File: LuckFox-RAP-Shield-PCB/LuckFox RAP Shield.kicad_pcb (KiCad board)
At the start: 2 copper layers, 45 x 62.6 mm, 8 parts, among them J1 LuckFox_Pico_Mini_Connector, J2 External_5V_Input_from_Buck_M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, U2 W5500_Ethernet_Module_DNP_on_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

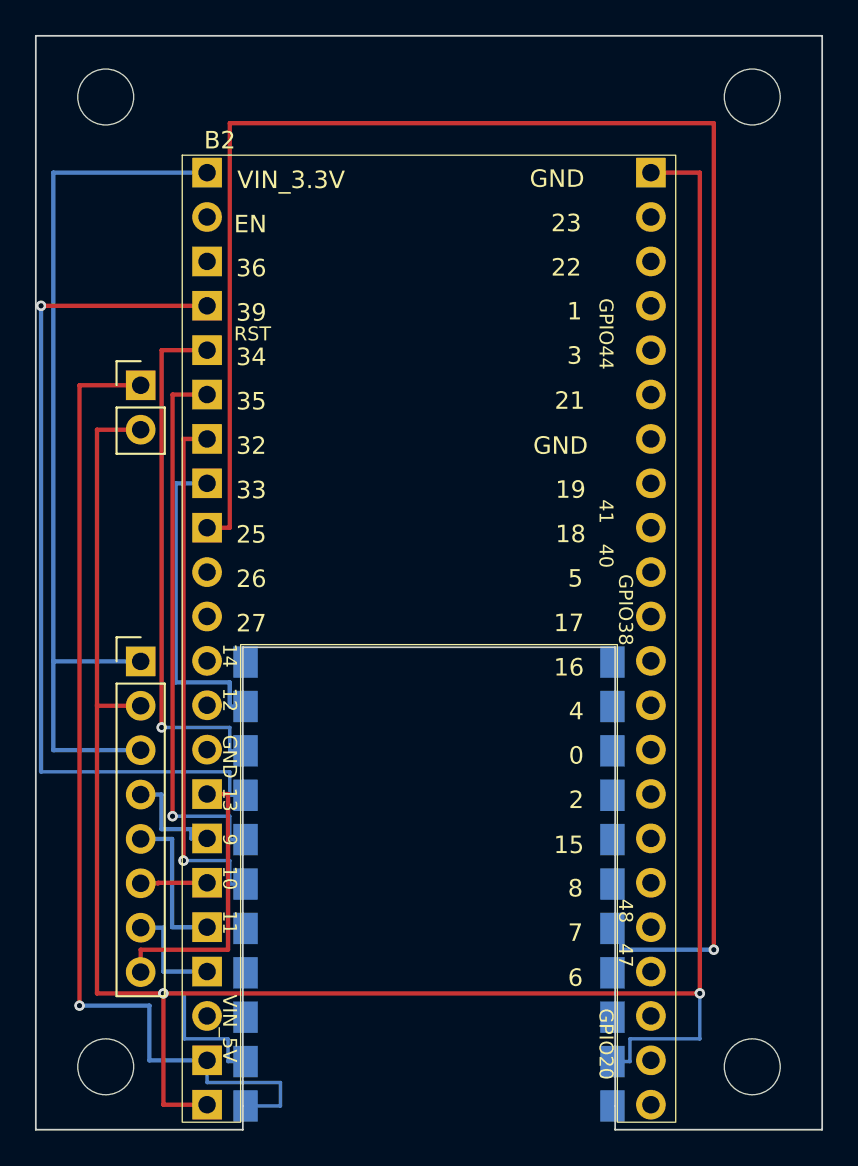
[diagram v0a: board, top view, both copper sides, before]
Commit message: Cut the real LuckFox nesting slot into the board outline, reroute GND/+5V_RAIL around it
LuckFox Pico Mini has an SD card slot, so it can't sit flush -- it
needs to actually nest into a cut opening in the shield (castellated
edge pads lap-solder where the module's edge meets the shield at the
slot boundary), not just be surface-soldered on top. The J1
footprint's own U-shaped Edge.Cuts lines already describe this slot
correctly, but its description explicitly warns "it is not
automatically merged with your board outline" -- and it never was.
Added the 3 missing lines to the top-level board outline so the slot
is now real (confirmed by re-deriving the closed outline: main
outline -> up J1's right edge -> across its top -> down its left
edge -> back to the main outline's own bottom notch).

Two nets previously ran straight through where that slot now is:
- GND's main trunk (116.5,129.8)-(151,129.8) crossed the entire
  21.3mm width of it. Rerouted above it instead: north to Y=99.34
  (clear of J2's pads to the south and B2/DATA_RDY's pins to the
  south-east), across on B.Cu (avoiding SPI0's F.Cu lanes at
  X=120.2/120.825/121.45, which occupy this same row), back down to
  the original via at (151,129.8) on the east side.
- +5V_RAIL's approach into J1.1 jogged out to X=127, well inside the
  slot, before turning back to the pad at X=125. Straightened to a
  short stub from X=124.1 (matching the established SPI0-style
  approach lane), only 0.15mm past the slot's real edge -- consistent
  with how J1's other pads (castellated, meant to straddle the edge)
  are already approached.

The short stubs already reaching J1's other pads (SPI0, DATA_RDY,
SLAVE_RDY_OUT, GND's other two J1 connections) were left as-is --
each only overhangs ~0.15-0.9mm past the real edge to reach a pad
that's itself meant to sit at that edge, same as J1's existing
castellated-pad DRU exception already covers for copper clearance.

Re-verified the new routing offline against every existing pad,
t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
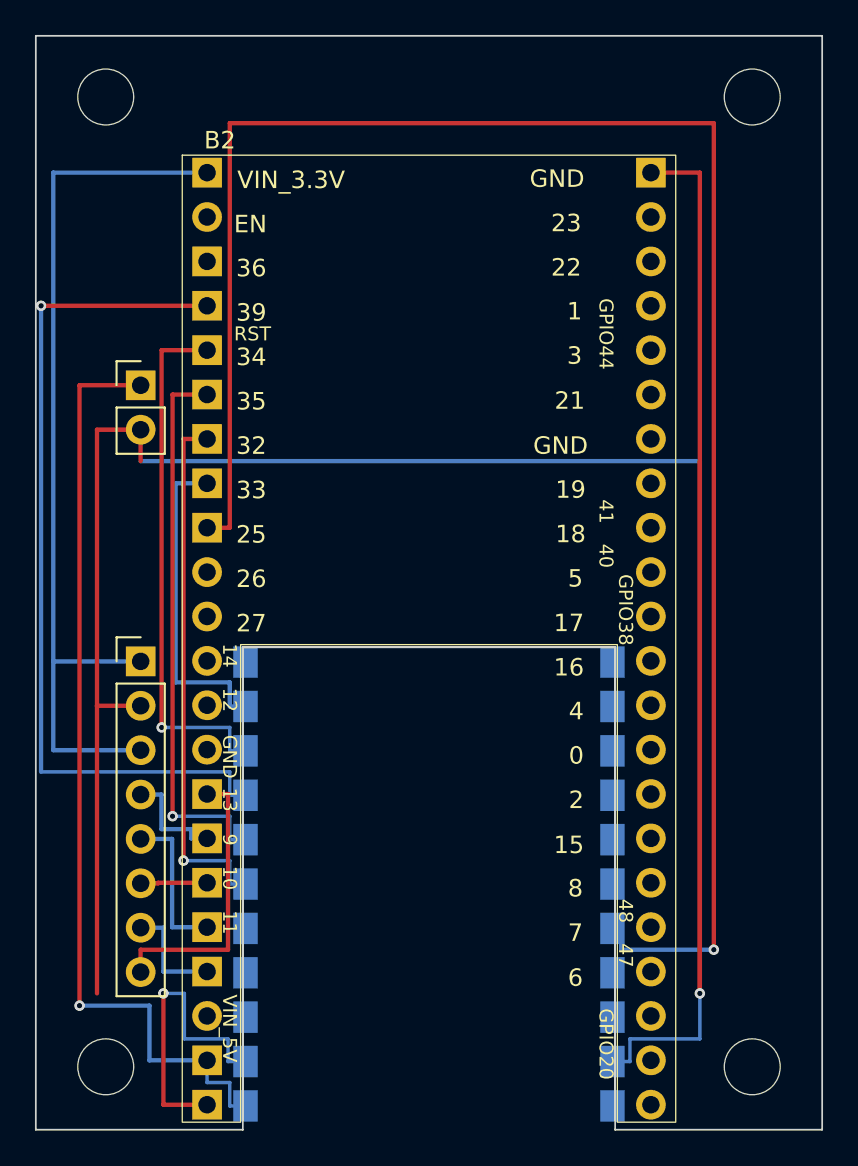
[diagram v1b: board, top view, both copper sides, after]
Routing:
- net GND: track 147.9 -> 177.7 mm
- net +5V_RAIL: track 58.2 -> 54.2 mm
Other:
- outline, holes or cut-outs redrawn
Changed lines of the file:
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@@
+	)
+	(gr_line
+		(start 146.15 136.24)
+		(end 146.15 109.99)
+		(stroke
+			(width 0.1)
+			(type solid)
+		)
+		(layer "Edge.Cuts")
+	)
+	(gr_line
+		(start 146.15 109.99)
+		(end 124.85 109.99)
+		(stroke
+			(width 0.1)
+			(type solid)
+		)
+		(layer "Edge.Cuts")
+	)
+	(gr_line
+		(start 124.85 109.99)
+		(end 124.85 136.24)
+		(stroke
+			(width 0.1)
+			(type solid)
+		)
+		(layer "Edge.Cuts")
 	)
 	(gr_line
@@
 	)
 	(segment
-		(start 127 134.9)
-		(end 127 136.24)
-		(width 0.2)
-		(layer "B.Cu")
-		(net "+5V_RAIL")
-	)
-	(segment
 		(start 119.5 133.63)
 		(end 122.8 133.63)
@@
 	)
 	(segment
-		(start 127 136.24)
-		(end 125 136.24)
-		(width 0.2)
-		(layer "B.Cu")
-		(net "+5V_RAIL")
-	)
-	(segment
-		(start 122.8 134.9)
-		(end 127 134.9)
-		(width 0.2)
-		(layer "B.Cu")
-		(net "+5V_RAIL")
-	)
-	(segment
 		(start 115.5 130.5)
 		(end 119.5 130.5)
@@
 	)
 	(segment
-		(start 116.5 129.8)
-		(end 151 129.8)
-		(width 0.25)
-		(layer "F.Cu")
-		(net "GND")
-	)
-	(segment
 		(start 120.3 129.8)
 		(end 120.3 136.17)
@@
 		(net "Net-(B2-GPIO16_SLAVE_RDY_OUT)")
 	)
+	(segment
+		(start 119.0 97.54)
+		(end 119.0 99.34)
+		(width 0.25)
+		(layer "F.Cu")
+		(net "GND")
+	)
+	(segment
+		(start 119.0 99.34)
+		(end 151.0 99.34)
+		(width 0.25)
+		(layer "B.Cu")
+		(net "GND")
+	)
+	(segment
+		(start 151.0 99.34)
+		(end 151.0 129.8)
+		(width 0.25)
+		(layer "F.Cu")
+		(net "GND")
+	)
+	(segment
+		(start 122.8 134.9)
+		(end 124.1 134.9)
+		(width 0.2)
+		(layer "B.Cu")
+		(net "+5V_RAIL")
+	)
+	(segment
+		(start 124.1 134.9)
+		(end 124.1 136.24)
+		(width 0.2)
+		(layer "B.Cu")
+		(net "+5V_RAIL")
+	)
+	(segment
+		(start 124.1 136.24)
+		(end 125.0 136.24)
+		(width 0.2)
+		(layer "B.Cu")
+		(net "+5V_RAIL")
+	)
 	(embedded_fonts no)

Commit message: Fix invalid outline, restore broken GND connection, and clear J1 stub tracks of the real edge
Three separate bugs from the last commit, all found via real DRC:

1. invalid_outline (self-intersecting / not closed): the 3 new
   top-level slot lines duplicated J1's own footprint-local copies of
   the exact same geometry -- two overlapping descriptions of the same
   boundary confuse the outline builder. Removed J1's local copies now
   that the real ones exist at the top level.

2. Unconnected GND: removing the old full-width trunk also removed the
   only link from (116.5,129.8) to the via at (120.3,129.8) -- which
   is a mid-span tap, not an endpoint, so it doesn't show up as broken
   until connectivity is actually walked. That via carries J1's left
   GND pad and one of B2's own GND branches. Restored the short
   (116.5,129.8)-(120.3,129.8) segment (west of the slot, was never
   part of the problem) to reconnect it.

3. copper_edge_clearance (7x): now that the slot is a real cutout,
   every short stub reaching into a J1 pad (SPI0's four signals,
   DATA_RDY, SLAVE_RDY_OUT, GND, +5V_RAIL) technically crossed the new
   edge to reach the pad's center. Rather than extend the J1
   castellated-pad DRU exception to cover tracks too, shortened each
   stub to stop just inside the real edge (X=124.8 for the left
   column, X=146.2 for the right) -- still well within the target
   pad's own footprint (which already legitimately overhangs the edge
   per the existing exception), so the connection completes through
   the pad's own copper without the track itself crossing the boundary.
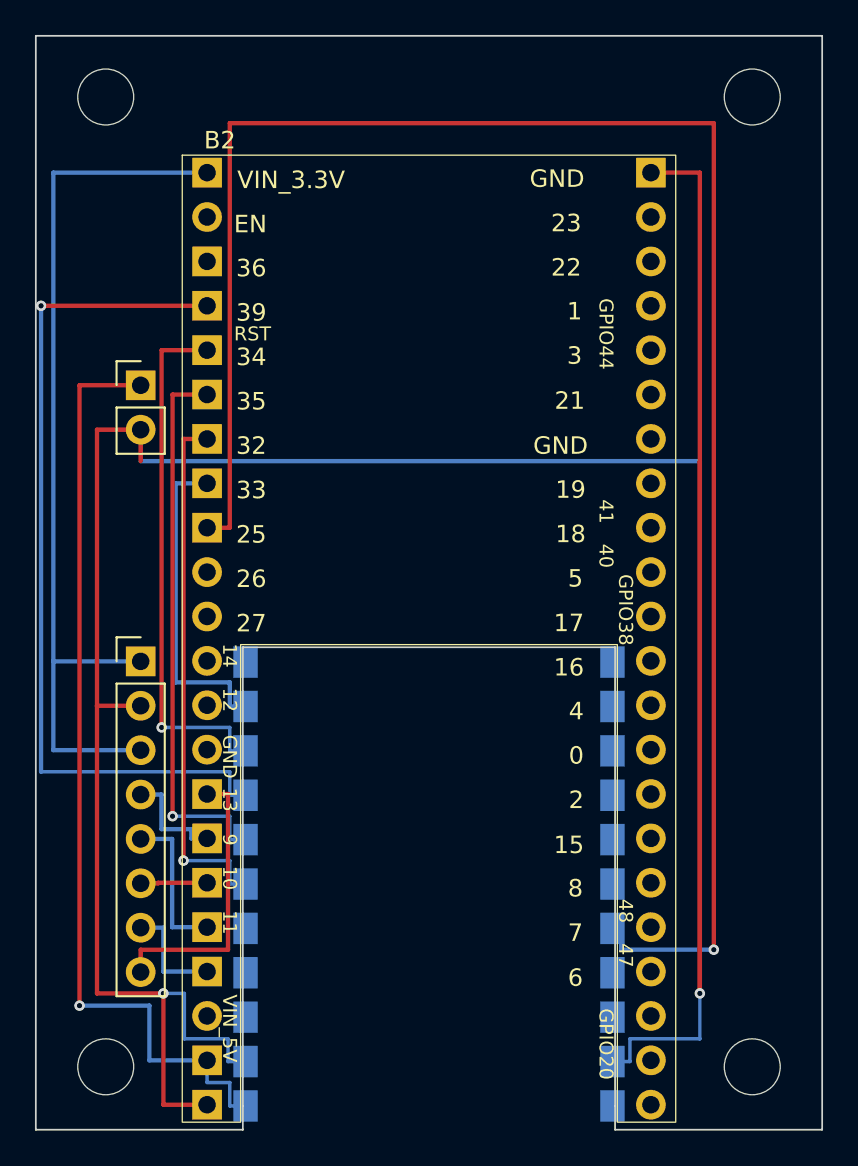
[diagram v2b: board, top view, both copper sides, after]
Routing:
- net GND: track 177.7 -> 181.1 mm
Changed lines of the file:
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@@
 		(attr smd)
 		(duplicate_pad_numbers_are_jumpers no)
-		(fp_line
-			(start -0.15 -0.15)
-			(end 21.15 -0.15)
-			(stroke
-				(width 0.1)
-				(type solid)
-			)
-			(layer "Edge.Cuts")
-		)
-		(fp_line
-			(start -0.15 26.1)
-			(end -0.15 -0.15)
-			(stroke
-				(width 0.1)
-				(type solid)
-			)
-			(layer "Edge.Cuts")
-		)
-		(fp_line
-			(start 21.15 -0.15)
-			(end 21.15 26.1)
-			(stroke
-				(width 0.1)
-				(type solid)
-			)
-			(layer "Edge.Cuts")
-		)
 		(fp_rect
 			(start -1 -1)
@@
 	(segment
 		(start 124 133.7)
-		(end 125 133.7)
+		(end 124.8 133.7)
 		(width 0.2)
 		(layer "B.Cu")
@@
 	(segment
 		(start 147 133.7)
-		(end 146 133.7)
+		(end 146.2 133.7)
 		(width 0.2)
 		(layer "B.Cu")
@@
 	(segment
 		(start 124.1 118.46)
-		(end 125 118.46)
+		(end 124.8 118.46)
 		(width 0.2)
 		(layer "B.Cu")
@@
 	(segment
 		(start 124.1 115.92)
-		(end 125 115.92)
+		(end 124.8 115.92)
 		(width 0.2)
 		(layer "B.Cu")
@@
 	(segment
 		(start 124.1 121)
-		(end 125 121)
+		(end 124.8 121.0)
 		(width 0.2)
 		(layer "B.Cu")
@@
 	(segment
 		(start 124.1 123.54)
-		(end 125 123.54)
+		(end 124.8 123.54)
 		(width 0.2)
 		(layer "B.Cu")
@@
 	(segment
 		(start 124.1 113.38)
-		(end 125 113.38)
+		(end 124.8 113.38)
 		(width 0.25)
 		(layer "B.Cu")
@@
 	(segment
 		(start 146.5 126.08)
-		(end 146 126.08)
+		(end 146.2 126.08)
 		(width 0.25)
 		(layer "B.Cu")
@@
 	(segment
 		(start 124.1 136.24)
-		(end 125.0 136.24)
+		(end 124.8 136.24)
 		(width 0.2)
 		(layer "B.Cu")
 		(net "+5V_RAIL")
 	)
+	(segment
+		(start 116.5 129.8)
+		(end 120.3 129.8)
+		(width 0.25)
+		(layer "F.Cu")
+		(net "GND")
+	)
 	(embedded_fonts no)

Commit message: Account for track width in J1 stub margins, add missing GND transition vias
Two more bugs from the last fix, both confirmed by real DRC:

1. copper_edge_clearance still fired on all 8 stubs -- shortening them
   to end at the edge coordinate (124.8/146.2) only moved the
   *centerline* clear of the boundary, not the actual copper (which
   extends another 0.1-0.125mm past the centerline for a 0.2-0.25mm
   track). Moved the endpoints further in (124.6 / 146.4) so the full
   copper width -- not just the centerline -- stays on the real board
   side, still comfortably inside the target pad's own footprint.

2. GND's detour (F.Cu -> B.Cu -> F.Cu at Y=99.34) never actually
   connected across those layer transitions -- a segment ending on one
   layer and another starting on a different layer at the same
   coordinate don't connect without a via bridging them there. Added
   the two missing vias at (119,99.34) and (151,99.34).
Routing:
- net GND: track 181.1 -> 180.7 mm, vias 2 -> 4
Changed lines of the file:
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@@
 	(segment
 		(start 124 133.7)
-		(end 124.8 133.7)
+		(end 124.6 133.7)
 		(width 0.2)
 		(layer "B.Cu")
@@
 	(segment
 		(start 147 133.7)
-		(end 146.2 133.7)
+		(end 146.4 133.7)
 		(width 0.2)
 		(layer "B.Cu")
@@
 	(segment
 		(start 124.1 118.46)
-		(end 124.8 118.46)
+		(end 124.6 118.46)
 		(width 0.2)
 		(layer "B.Cu")
@@
 	(segment
 		(start 124.1 115.92)
-		(end 124.8 115.92)
+		(end 124.6 115.92)
 		(width 0.2)
 		(layer "B.Cu")
@@
 	(segment
 		(start 124.1 121)
-		(end 124.8 121.0)
+		(end 124.6 121.0)
 		(width 0.2)
 		(layer "B.Cu")
@@
 	(segment
 		(start 124.1 123.54)
-		(end 124.8 123.54)
+		(end 124.6 123.54)
 		(width 0.2)
 		(layer "B.Cu")
@@
 	(segment
 		(start 124.1 113.38)
-		(end 124.8 113.38)
+		(end 124.6 113.38)
 		(width 0.25)
 		(layer "B.Cu")
@@
 	(segment
 		(start 146.5 126.08)
-		(end 146.2 126.08)
+		(end 146.4 126.08)
 		(width 0.25)
 		(layer "B.Cu")
@@
 	(segment
 		(start 124.1 136.24)
-		(end 124.8 136.24)
+		(end 124.6 136.24)
 		(width 0.2)
 		(layer "B.Cu")
@@
 		(net "GND")
 	)
+	(via
+		(at 119.0 99.34)
+		(size 0.6)
+		(drill 0.3)
+		(layers "F.Cu" "B.Cu")
+		(net "GND")
+	)
+	(via
+		(at 151.0 99.34)
+		(size 0.6)
+		(drill 0.3)
+		(layers "F.Cu" "B.Cu")
+		(net "GND")
+	)
